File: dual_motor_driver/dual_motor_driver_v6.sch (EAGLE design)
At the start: 86 parts, among them IC1 MCP602SN

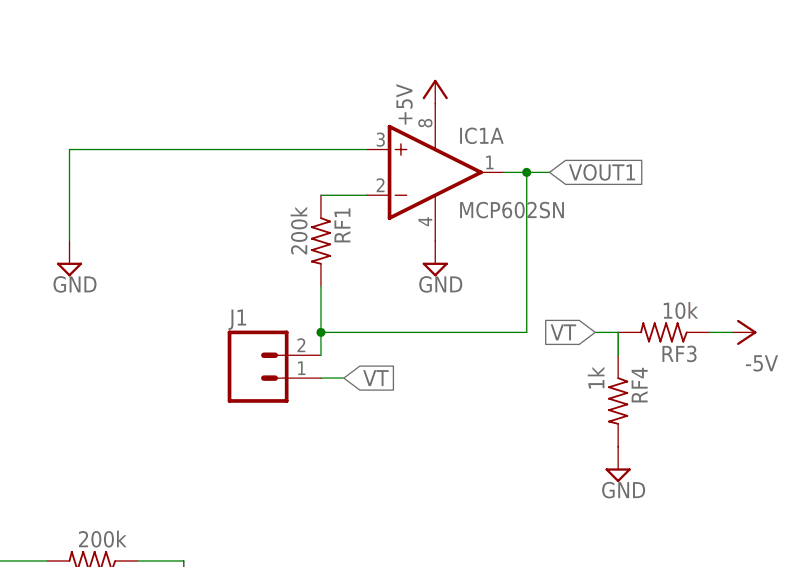
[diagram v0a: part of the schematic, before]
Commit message: fixed tension sensor amplifier
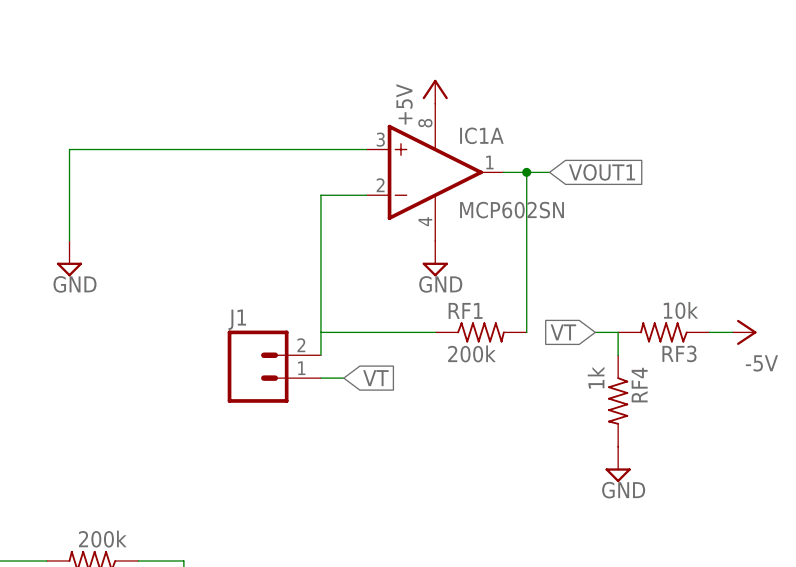
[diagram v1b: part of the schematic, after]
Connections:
- removed net N$76: IC1A.-IN, RF1.1
- new net N$52: IC1A.-IN, J1.2, RF1.1
- net VOUT1: no longer J1.2
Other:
- moved on the sheet: RF1
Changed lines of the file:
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@@
 <instance part="SUPPLY8" gate="GND" x="142.24" y="68.58"/>
 <instance part="SUPPLY9" gate="GND" x="101.6" y="68.58"/>
-<instance part="RF1" gate="G$1" x="129.54" y="71.12" rot="R270"/>
+<instance part="RF1" gate="G$1" x="147.32" y="60.96"/>
 <instance part="J1" gate="G$1" x="121.92" y="55.88"/>
 <instance part="J2" gate="G$1" x="81.28" y="20.32"/>
@@
 </segment>
 </net>
-<net name="N$76" class="0">
-<segment>
-<pinref part="IC1" gate="A" pin="-IN"/>
-<pinref part="RF1" gate="G$1" pin="1"/>
-<wire x1="129.54" y1="76.2" x2="134.62" y2="76.2" width="0.1524" layer="91"/>
-</segment>
-</net>
 <net name="VOUT1" class="0">
 <segment>
-<pinref part="RF1" gate="G$1" pin="2"/>
-<wire x1="129.54" y1="66.04" x2="129.54" y2="60.96" width="0.1524" layer="91"/>
-<wire x1="129.54" y1="60.96" x2="152.4" y2="60.96" width="0.1524" layer="91"/>
 <pinref part="IC1" gate="A" pin="OUT"/>
 <wire x1="152.4" y1="60.96" x2="152.4" y2="78.74" width="0.1524" layer="91"/>
 <wire x1="149.86" y1="78.74" x2="152.4" y2="78.74" width="0.1524" layer="91"/>
-<pinref part="J1" gate="G$1" pin="2"/>
 <wire x1="152.4" y1="78.74" x2="154.94" y2="78.74" width="0.1524" layer="91"/>
-<wire x1="129.54" y1="58.42" x2="129.54" y2="60.96" width="0.1524" layer="91"/>
 <label x="154.94" y="78.74" size="1.778" layer="95" xref="yes"/>
-<junction x="129.54" y="60.96"/>
 <junction x="152.4" y="78.74"/>
+<pinref part="RF1" gate="G$1" pin="2"/>
 </segment>
 <segment>
@@
 </segment>
 </net>
+<net name="N$52" class="0">
+<segment>
+<pinref part="J1" gate="G$1" pin="2"/>
+<wire x1="129.54" y1="58.42" x2="129.54" y2="60.96" width="0.1524" layer="91"/>
+<pinref part="RF1" gate="G$1" pin="1"/>
+<wire x1="142.24" y1="60.96" x2="129.54" y2="60.96" width="0.1524" layer="91"/>
+<pinref part="IC1" gate="A" pin="-IN"/>
+<wire x1="129.54" y1="60.96" x2="129.54" y2="76.2" width="0.1524" layer="91"/>
+<wire x1="129.54" y1="76.2" x2="134.62" y2="76.2" width="0.1524" layer="91"/>
+</segment>
+</net>

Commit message: last update, working
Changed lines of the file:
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@@
 <wire x1="134.62" y1="81.28" x2="101.6" y2="81.28" width="0.1524" layer="91"/>
 <wire x1="101.6" y1="81.28" x2="101.6" y2="71.12" width="0.1524" layer="91"/>
+<junction x="134.62" y="81.28"/>
 </segment>
 <segment>
@@
 <wire x1="162.56" y1="60.96" x2="160.02" y2="60.96" width="0.1524" layer="91"/>
 <label x="160.02" y="60.96" size="1.778" layer="95" rot="R180" xref="yes"/>
+<junction x="162.56" y="60.96"/>
 </segment>
 <segment>
@@
 <wire x1="129.54" y1="60.96" x2="129.54" y2="76.2" width="0.1524" layer="91"/>
 <wire x1="129.54" y1="76.2" x2="134.62" y2="76.2" width="0.1524" layer="91"/>
-</segment>
-</net>
+<junction x="129.54" y="60.96"/>
+<junction x="134.62" y="76.2"/>
+</segment>
+</net>
